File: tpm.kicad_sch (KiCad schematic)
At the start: 0 parts

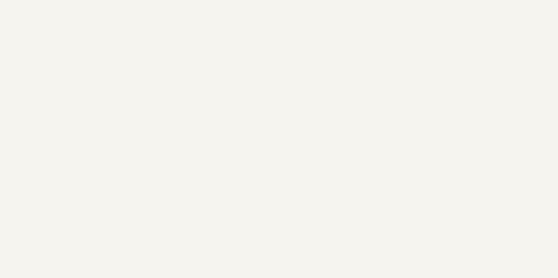
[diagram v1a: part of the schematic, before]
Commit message: Add TPM connector
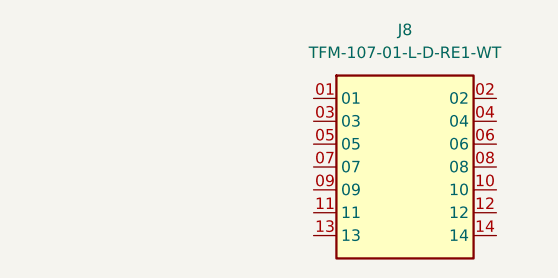
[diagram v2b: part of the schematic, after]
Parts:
- added J8: TFM-107-01-X-D-RE1-WT, antmicro-footprints:Socket_Samtec_TFM_2x7_TFM-107-01-X-D-RE1-WT, symbol antmicroB2BConnectors:Socket_Samtec_TFM_2x7_TFM-107-01-X-D-RE1-WT
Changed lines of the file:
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@@
+		)
+	)
+	(symbol
+		(lib_id "antmicroB2BConnectors:Socket_Samtec_TFM_2x7_TFM-107-01-X-D-RE1-WT")
+		(at 175.26 87.63 0)
+		(unit 1)
+		(exclude_from_sim no)
+		(in_bom yes)
+		(on_board yes)
+		(dnp no)
+		(fields_autoplaced yes)
+		(property "Reference" "J8"
+			(at 185.42 80.01 0)
+			(effects
+				(font
+					(size 1.27 1.27)
+					(thickness 0.15)
+				)
+			)
+		)
+		(property "Value" "TFM-107-01-X-D-RE1-WT"
+			(at 210.82 95.25 0)
+			(effects
+				(font
+					(size 1.27 1.27)
+					(thickness 0.15)
+				)
+				(justify left bottom)
+				(hide yes)
+			)
+		)
+		(property "Footprint" "antmicro-footprints:Socket_Samtec_TFM_2x7_TFM-107-01-X-D-RE1-WT"
+			(at 210.82 97.79 0)
+			(effects
+				(font
+					(size 1.27 1.27)
+					(thickness 0.15)
+				)
+				(justify left bottom)
+				(hide yes)
+			)
+		)
+		(property "Datasheet" "https://mm.digikey.com/Volume0/opasdata/d220001/medias/docus/6129/tfm-1xx-xx-xxx-d-xxx-x-xx-mkt.pdf"
+			(at 210.82 100.33 0)
+			(effects
+				(font
+					(size 1.27 1.27)
+					(thickness 0.15)
+				)
+				(justify left bottom)
+				(hide yes)
+			)
+		)
+		(property "Description" "CONN HEADER R/A 14POS 1.27MM"
+			(at 210.82 102.87 0)
+			(effects
+				(font
+					(size 1.27 1.27)
+					(thickness 0.15)
+				)
+				(justify left bottom)
+				(hide yes)
+			)
+		)
+		(property "MPN" "TFM-107-01-L-D-RE1-WT"
+			(at 185.42 82.55 0)
+			(effects
+				(font
+					(size 1.27 1.27)
+					(thickness 0.15)
+				)
+			)
+		)
+		(property "Manufacturer" "Samtec"
+			(at 210.82 105.41 0)
+			(effects
+				(font
+					(size 1.27 1.27)
+					(thickness 0.15)
+				)
+				(justify left bottom)
+				(hide yes)
+			)
+		)
+		(property "Author" "Antmicro"
+			(at 210.82 107.95 0)
+			(effects
+				(font
+					(size 1.27 1.27)
+					(thickness 0.15)
+				)
+				(justify left bottom)
+				(hide yes)
+			)
+		)
+		(property "License" "Apache-2.0"
+			(at 210.82 110.49 0)
+			(effects
+				(font
+					(size 1.27 1.27)
+					(thickness 0.15)
+				)
+				(justify left bottom)
+				(hide yes)
+			)
+		)
+		(pin "06"
+		)
+		(pin "12"
+		)
+		(pin "13"
+		)
+		(pin "11"
+		)
+		(pin "09"
+		)
+		(pin "07"
+		)
+		(pin "05"
+		)
+		(pin "03"
+		)
+		(pin "01"
+		)
+		(pin "02"
+		)
+		(pin "04"
+		)
+		(pin "14"
+		)
+		(pin "10"
+		)
+		(pin "08"
+		)
+		(instances
+			(project ""
+				(path "/5f636c45-3c15-4731-8931-4625e0dab7e4/757bd70a-5179-4368-9172-3adb38876975"
+					(reference "J8")
+					(unit 1)
+				)
+			)
 		)
 	)

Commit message: Annotate schematic
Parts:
- J8: footprint antmicro-footprints:Socket_Samtec_TFM_2x7_TFM-107-01-X-D-RE1-WT -> antmicro-footprints:Conn_Socket_Samtec_TFM_2x7_TFM-107-01-X-D-RE1-WT
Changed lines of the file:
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@@
 			)
 		)
-		(property "Footprint" "antmicro-footprints:Socket_Samtec_TFM_2x7_TFM-107-01-X-D-RE1-WT"
+		(property "Footprint" "antmicro-footprints:Conn_Socket_Samtec_TFM_2x7_TFM-107-01-X-D-RE1-WT"
 			(at 210.82 97.79 0)
 			(effects
@@
 			)
 		)
-		(pin "06"
+		(pin "2"
 		)
 		(pin "12"
@@
 		(pin "11"
 		)
-		(pin "09"
+		(pin "1"
 		)
-		(pin "07"
+		(pin "6"
 		)
-		(pin "05"
+		(pin "9"
 		)
-		(pin "03"
+		(pin "8"
 		)
-		(pin "01"
+		(pin "3"
 		)
-		(pin "02"
+		(pin "4"
 		)
-		(pin "04"
+		(pin "5"
 		)
 		(pin "14"
@@
 		(pin "10"
 		)
-		(pin "08"
+		(pin "7"
+		)
+		(pin "SH"
 		)
 		(instances

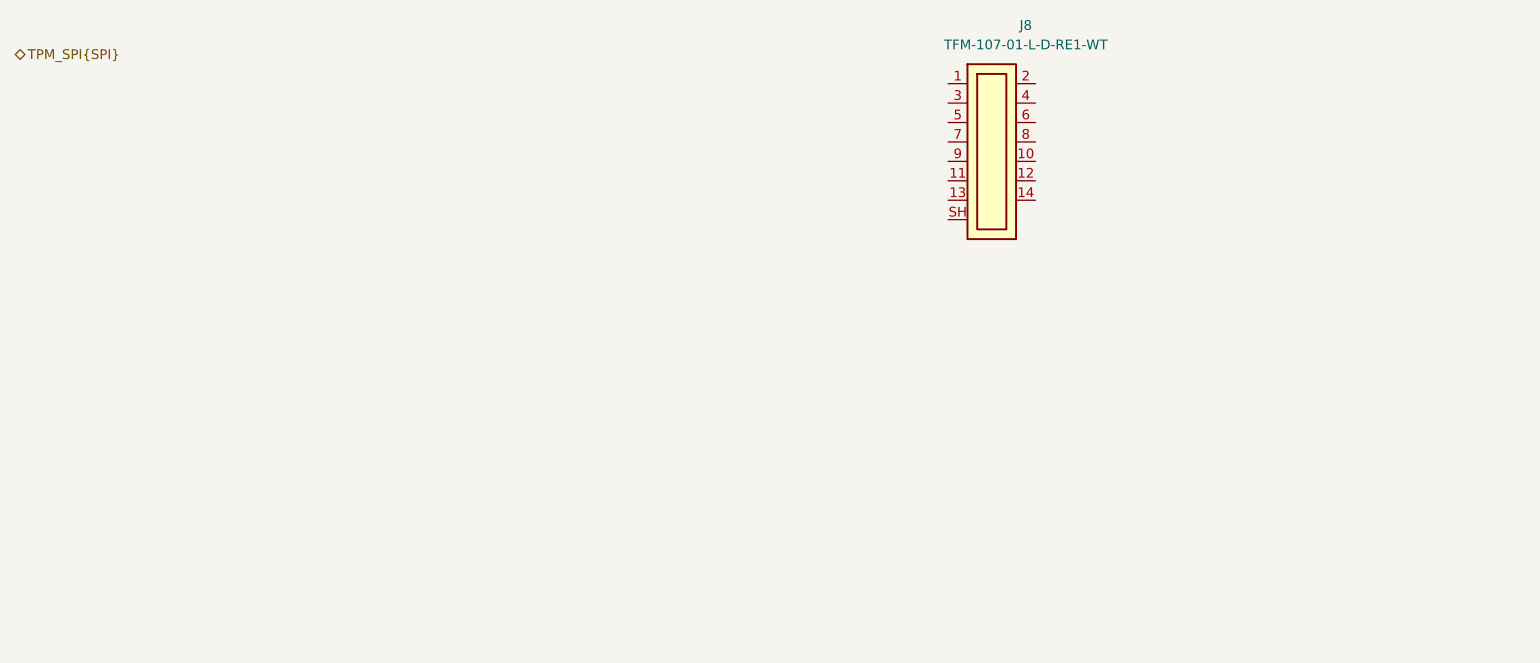
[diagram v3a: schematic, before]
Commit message: Changed A4 sheets to A3 and cleaned them up
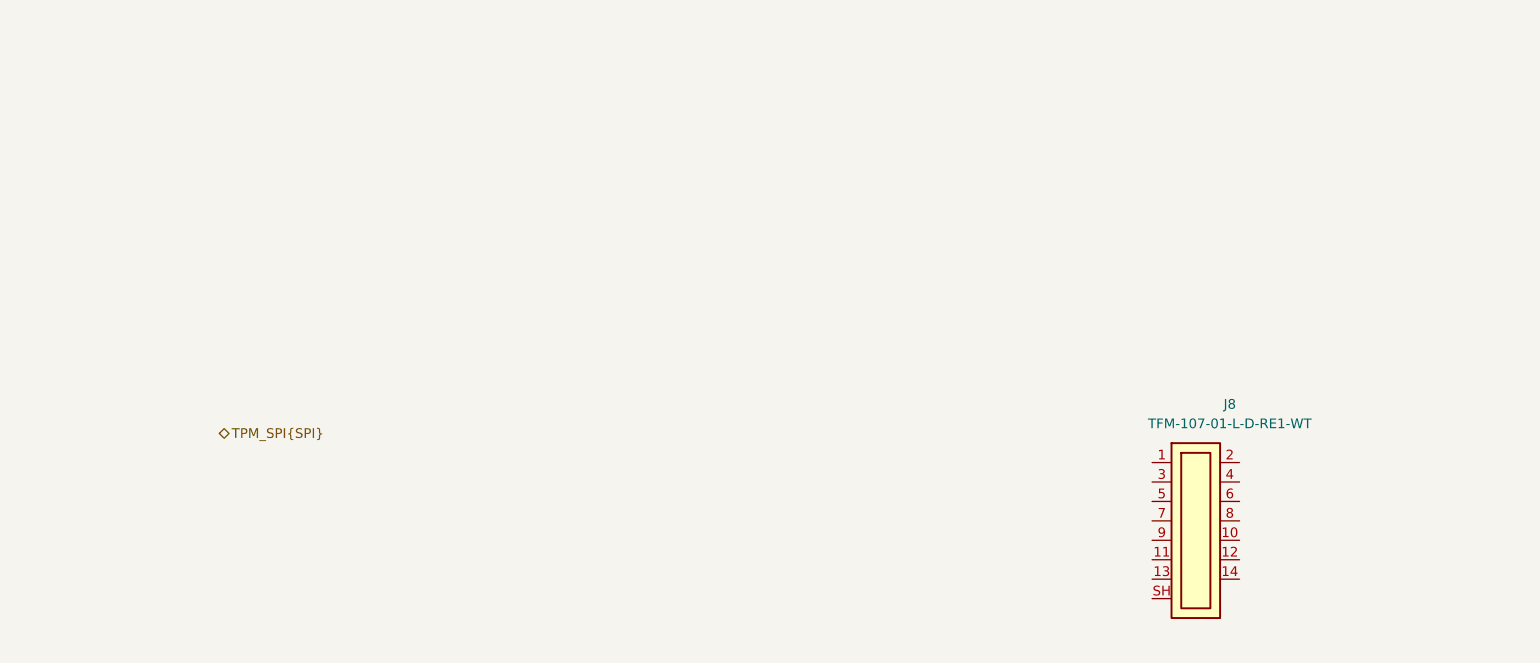
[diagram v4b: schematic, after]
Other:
- moved on the sheet: J8
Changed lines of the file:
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@@
 	(hierarchical_label "TPM_SPI{SPI}"
 		(shape bidirectional)
-		(at 53.34 83.82 0)
+		(at 80.01 133.35 0)
 		(effects
 			(font
@@
 	(symbol
 		(lib_id "antmicroB2BConnectors:Socket_Samtec_TFM_2x7_TFM-107-01-X-D-RE1-WT")
-		(at 175.26 87.63 0)
+		(at 201.93 137.16 0)
 		(unit 1)
 		(exclude_from_sim no)
@@
 		(fields_autoplaced yes)
 		(property "Reference" "J8"
-			(at 185.42 80.01 0)
+			(at 212.09 129.54 0)
 			(effects
 				(font
@@
 		)
 		(property "Value" "TFM-107-01-X-D-RE1-WT"
-			(at 210.82 95.25 0)
+			(at 237.49 144.78 0)
 			(effects
 				(font
@@
 		)
 		(property "Footprint" "antmicro-footprints:Conn_Socket_Samtec_TFM_2x7_TFM-107-01-X-D-RE1-WT"
-			(at 210.82 97.79 0)
+			(at 237.49 147.32 0)
 			(effects
 				(font
@@
 		)
 		(property "Datasheet" "https://mm.digikey.com/Volume0/opasdata/d220001/medias/docus/6129/tfm-1xx-xx-xxx-d-xxx-x-xx-mkt.pdf"
-			(at 210.82 100.33 0)
+			(at 237.49 149.86 0)
 			(effects
 				(font
@@
 		)
 		(property "Description" "CONN HEADER R/A 14POS 1.27MM"
-			(at 210.82 102.87 0)
+			(at 237.49 152.4 0)
 			(effects
 				(font
@@
 		)
 		(property "MPN" "TFM-107-01-L-D-RE1-WT"
-			(at 185.42 82.55 0)
+			(at 212.09 132.08 0)
 			(effects
 				(font
@@
 		)
 		(property "Manufacturer" "Samtec"
-			(at 210.82 105.41 0)
+			(at 237.49 154.94 0)
 			(effects
 				(font
@@
 		)
 		(property "Author" "Antmicro"
-			(at 210.82 107.95 0)
+			(at 237.49 157.48 0)
 			(effects
 				(font
@@
 		)
 		(property "License" "Apache-2.0"
-			(at 210.82 110.49 0)
+			(at 237.49 160.02 0)
 			(effects
 				(font

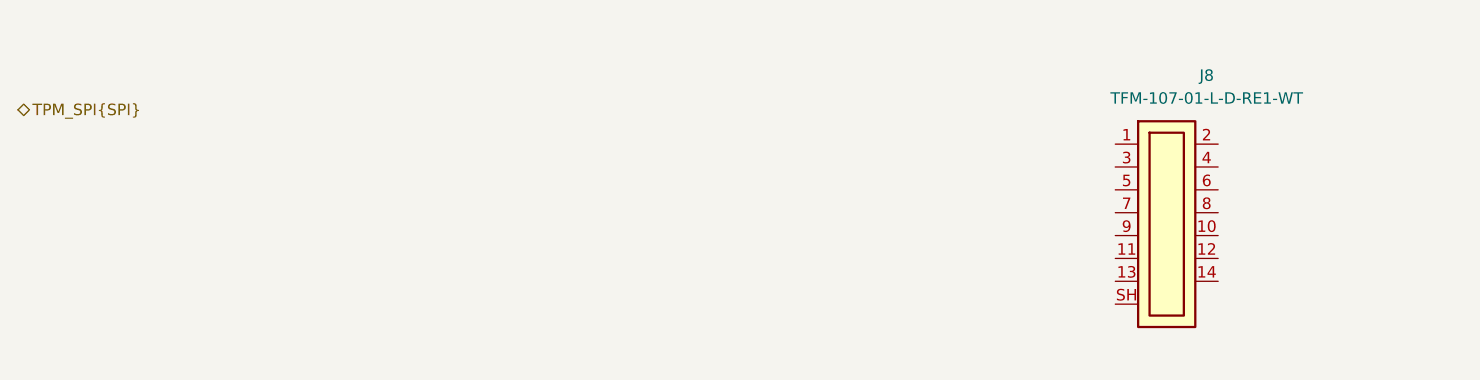
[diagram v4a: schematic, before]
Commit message: [#83335] Change TPM connector to 2x7 pin header and connect it
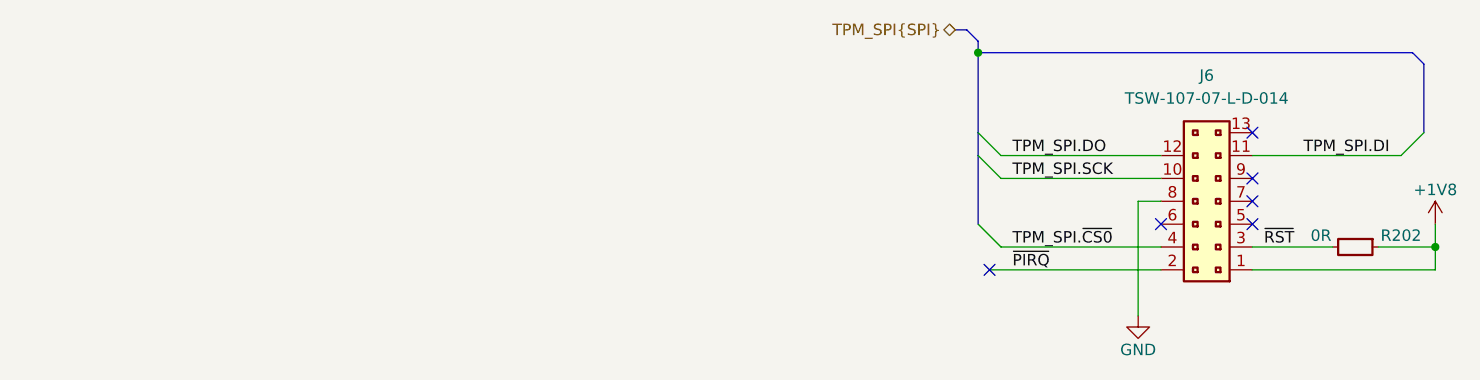
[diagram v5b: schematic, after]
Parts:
- removed J8: TFM-107-01-X-D-RE1-WT, antmicro-footprints:Conn_Socket_Samtec_TFM_2x7_TFM-107-01-X-D-RE1-WT, symbol antmicroB2BConnectors:Socket_Samtec_TFM_2x7_TFM-107-01-X-D-RE1-WT
- added J6: PinHeader_2x7_P2.54mm_Drill1.02mm_ TSW-107-07-L-D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, antmicro-footprints:PinHeader_2x7_P2.54mm_Drill1.02mm_TSW-107-07-L-D-014, symbol antmicroGenericPinHeaders:PinHeader_2x7_P2.54mm_Drill1.02mm_ TSW-107-07-L-D-014
- added R202: R_0R_0402, antmicro-footprints:R_0402_1005Metric, symbol antmicroResistors0402:R_0R_0402
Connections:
- new net +1V8: J6.1, R202.1
- new net GND: J6.8
- new net TPM_SPI.DI: J6.11
- new net TPM_SPI.DO: J6.12
- new net TPM_SPI.SCK: J6.10
- new net TPM_SPI.~{CS0}: J6.4
- new net ~{PIRQ}: J6.2
- new net ~{RST}: J6.3, R202.2
- no-connect marks 0 -> 6

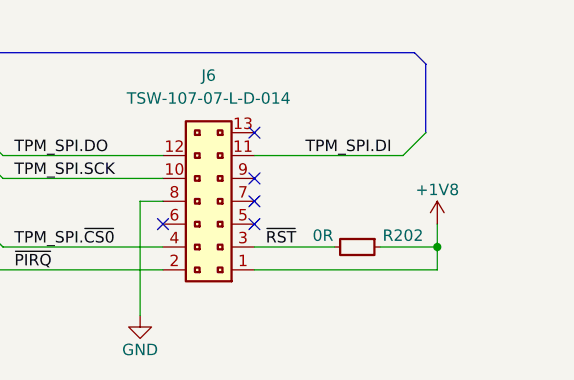
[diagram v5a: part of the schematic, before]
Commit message: [#83335] Connected RST of TPM to OSM
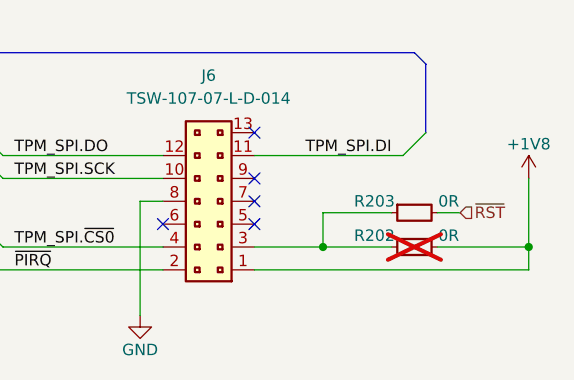
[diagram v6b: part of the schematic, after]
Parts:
- added R203: R_0R_0402, antmicro-footprints:R_0402_1005Metric, symbol antmicroResistors0402:R_0R_0402
- R202: now not fitted
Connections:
- net +1V8: now also R202.2; no longer R202.1
- net ~{RST}: now also R203.2; no longer J6.3, R202.2
- new net: J6.3, R202.1, R203.1

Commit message: [#83609] Reannotate board
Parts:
- renumbered J6 to J3, R203 to R144, R202 to R145
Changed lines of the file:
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@@
 		(dnp no)
 		(fields_autoplaced yes)
-		(property "Reference" "J6"
+		(property "Reference" "J3"
 			(at 212.09 129.54 0)
 			(effects
@@
 			(project ""
 				(path "/5f636c45-3c15-4731-8931-4625e0dab7e4/757bd70a-5179-4368-9172-3adb38876975"
-					(reference "J6")
+					(reference "J3")
 					(unit 1)
 				)
@@
 		(on_board yes)
 		(dnp no)
-		(property "Reference" "R203"
+		(property "Reference" "R144"
 			(at 230.505 143.51 0)
 			(effects
@@
 			(project "bmc-reference-carrier-board"
 				(path "/5f636c45-3c15-4731-8931-4625e0dab7e4/757bd70a-5179-4368-9172-3adb38876975"
-					(reference "R203")
+					(reference "R144")
 					(unit 1)
 				)
@@
 		(on_board yes)
 		(dnp no)
-		(property "Reference" "#PWR0289"
+		(property "Reference" "#PWR0103"
 			(at 262.89 143.51 0)
 			(effects
@@
 			(project "bmc-reference-carrier-board"
 				(path "/5f636c45-3c15-4731-8931-4625e0dab7e4/757bd70a-5179-4368-9172-3adb38876975"
-					(reference "#PWR0289")
+					(reference "#PWR0103")
 					(unit 1)
 				)
@@
 		(on_board yes)
 		(dnp no)
-		(property "Reference" "#PWR0261"
+		(property "Reference" "#PWR0102"
 			(at 213.36 158.75 0)
 			(effects
@@
 			(project ""
 				(path "/5f636c45-3c15-4731-8931-4625e0dab7e4/757bd70a-5179-4368-9172-3adb38876975"
-					(reference "#PWR0261")
+					(reference "#PWR0102")
 					(unit 1)
 				)
@@
 		(on_board yes)
 		(dnp yes)
-		(property "Reference" "R202"
+		(property "Reference" "R145"
 			(at 230.505 147.32 0)
 			(effects
@@
 			(project ""
 				(path "/5f636c45-3c15-4731-8931-4625e0dab7e4/757bd70a-5179-4368-9172-3adb38876975"
-					(reference "R202")
+					(reference "R145")
 					(unit 1)
 				)
